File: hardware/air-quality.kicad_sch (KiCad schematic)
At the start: 26 parts, among them J1 USB_C_Receptacle_USB2.0, Q1 UMH3N, U1 ME6211A33M3G-N, U2 CH340C, U3 ESP-12F, U4 SGP40, U5 HDC1080

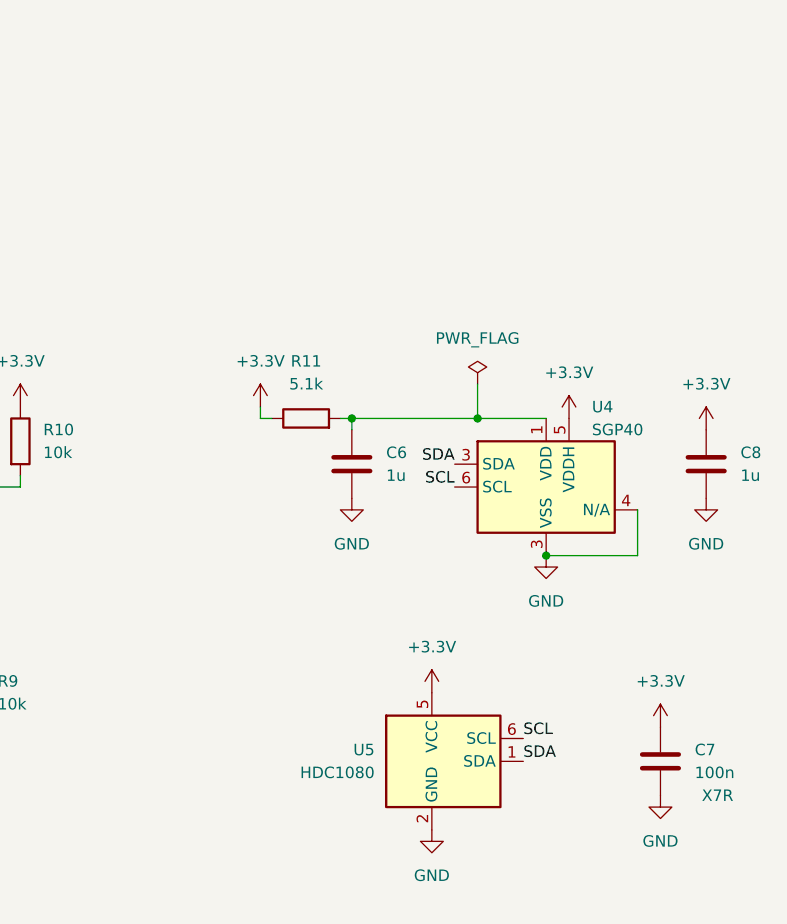
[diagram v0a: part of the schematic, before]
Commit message: Added display
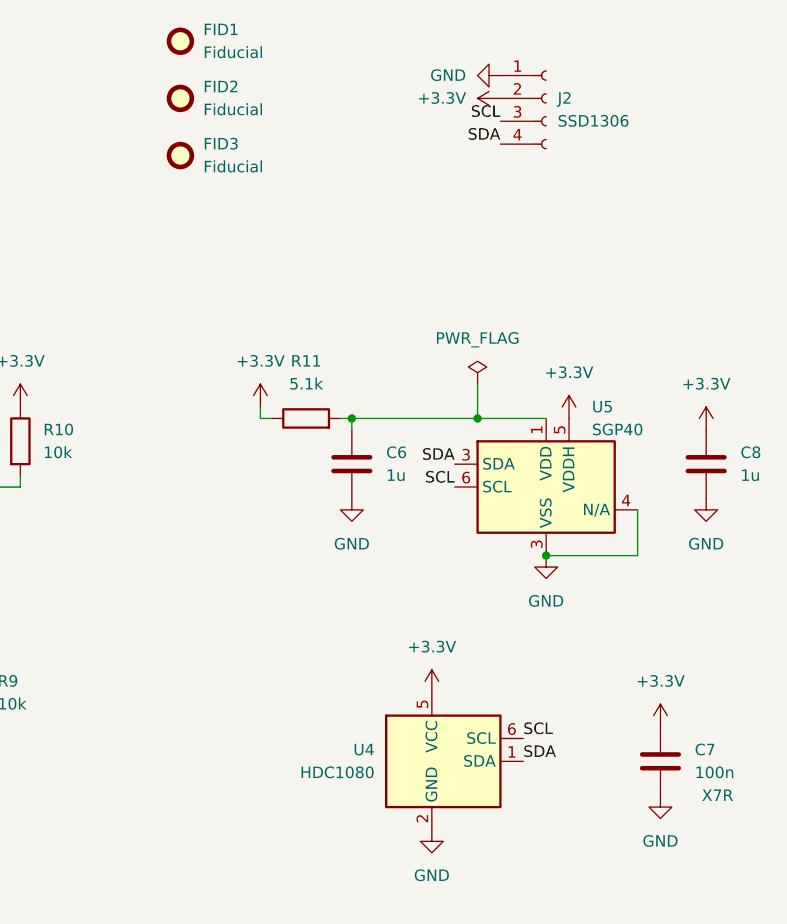
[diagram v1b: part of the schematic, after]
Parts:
- added FID1, FID2, FID3: Fiducial, Fiducial:Fiducial_0.5mm_Mask1mm, symbol Mechanical:Fiducial
- added J2: SSD1306, Connector_PinSocket_2.54mm:PinSocket_1x04_P2.54mm_Vertical, symbol Connector:Conn_01x04_Female
- renumbered U5 to U4, U4 to U5
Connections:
- net +3V3: now also J2.2 (Pin_2)
- net GND: now also J2.1 (Pin_1)
- net SCL: now also J2.3 (Pin_3)
- net SDA: now also J2.4 (Pin_4)

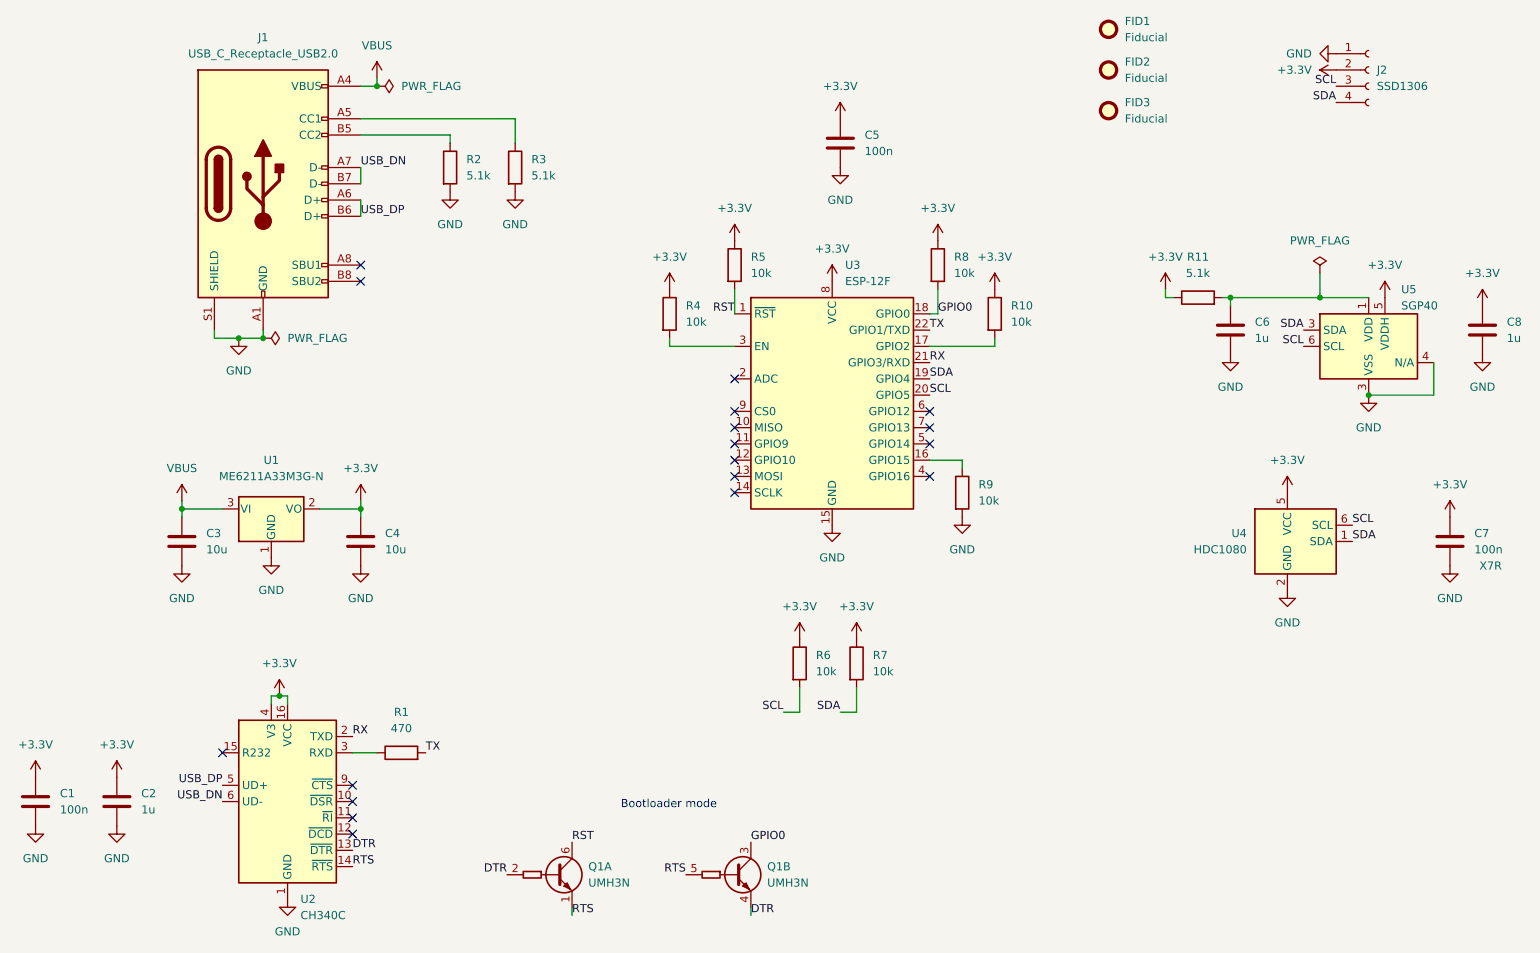
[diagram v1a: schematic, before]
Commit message: Update to KiCAD v8
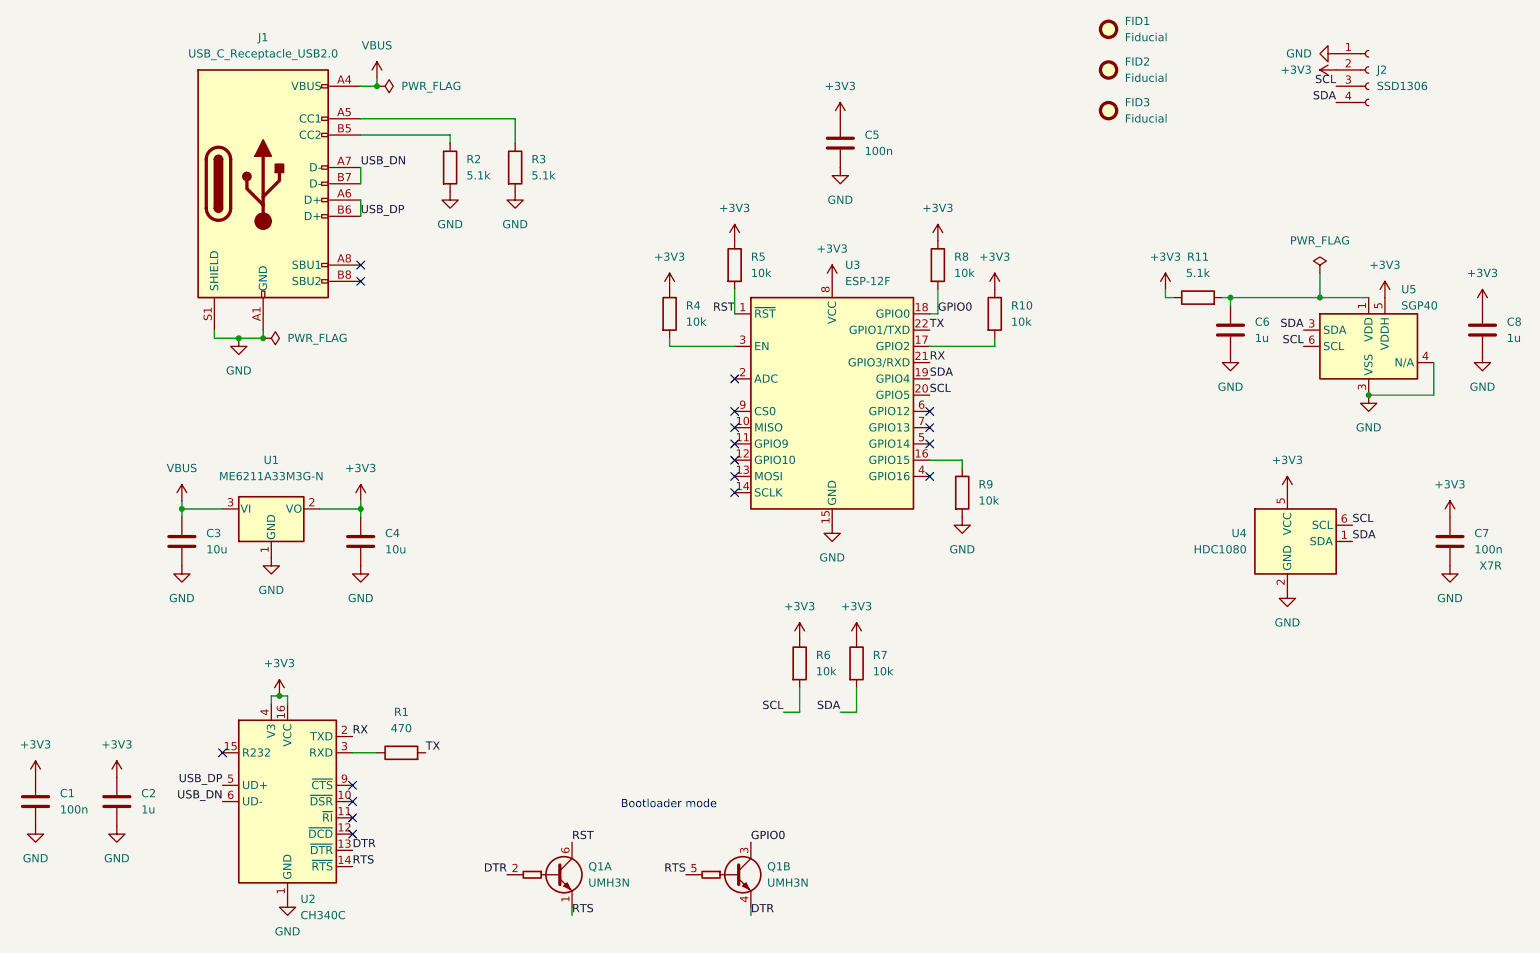
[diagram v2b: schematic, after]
